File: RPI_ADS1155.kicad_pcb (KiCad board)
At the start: 2 copper layers, 84.6 x 56 mm, 28 parts, among them J1 Raspberry_PI_4, J2 DIGITAL_BITS, SW1 SW_DIP_x04, SW2 SW_Push, SW3 SW_Push, U1 ADS1115IDGS

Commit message: Add files via upload
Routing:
- net /+3.3V: track 126.3 -> 244.3 mm, vias 0 -> 2
- net /AINO: track 26.8 -> 27.7 mm
- net /AIN1: track 29.1 -> 30.1 mm

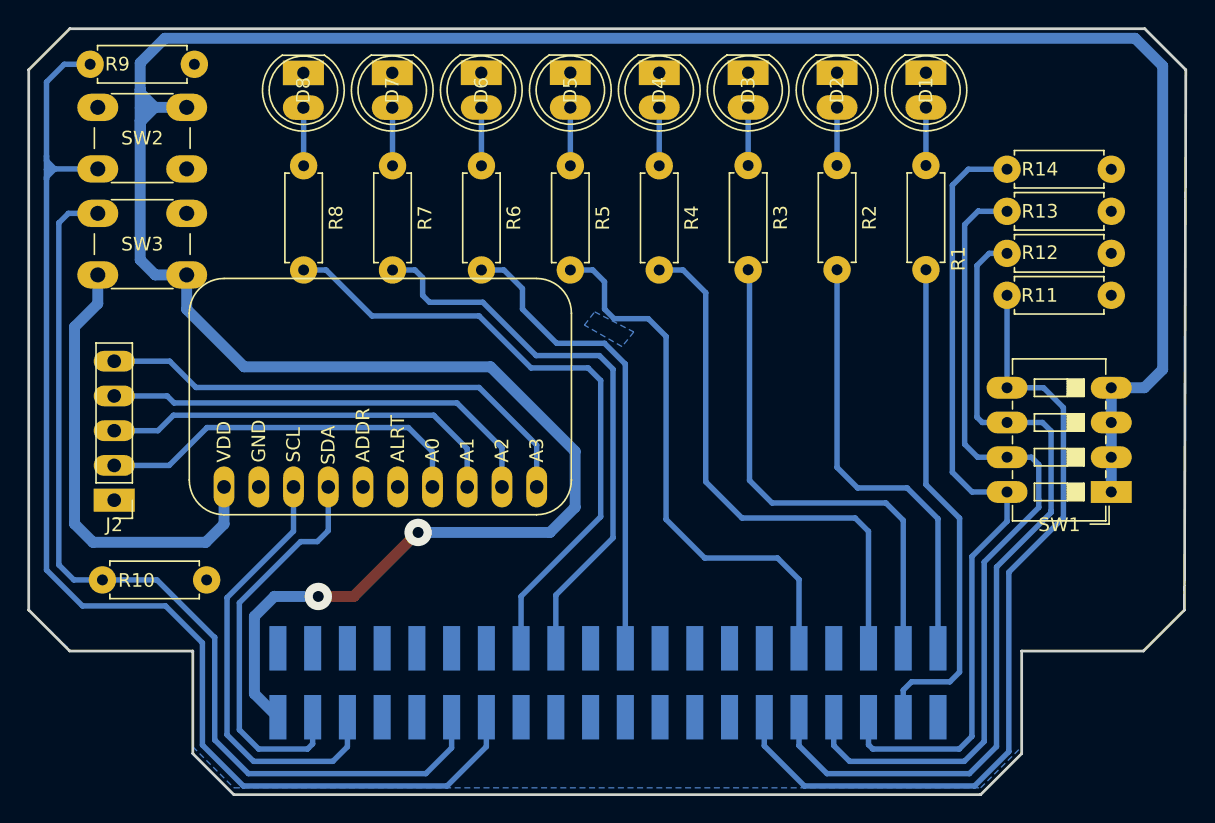
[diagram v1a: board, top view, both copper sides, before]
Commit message: Add UART connector and pins
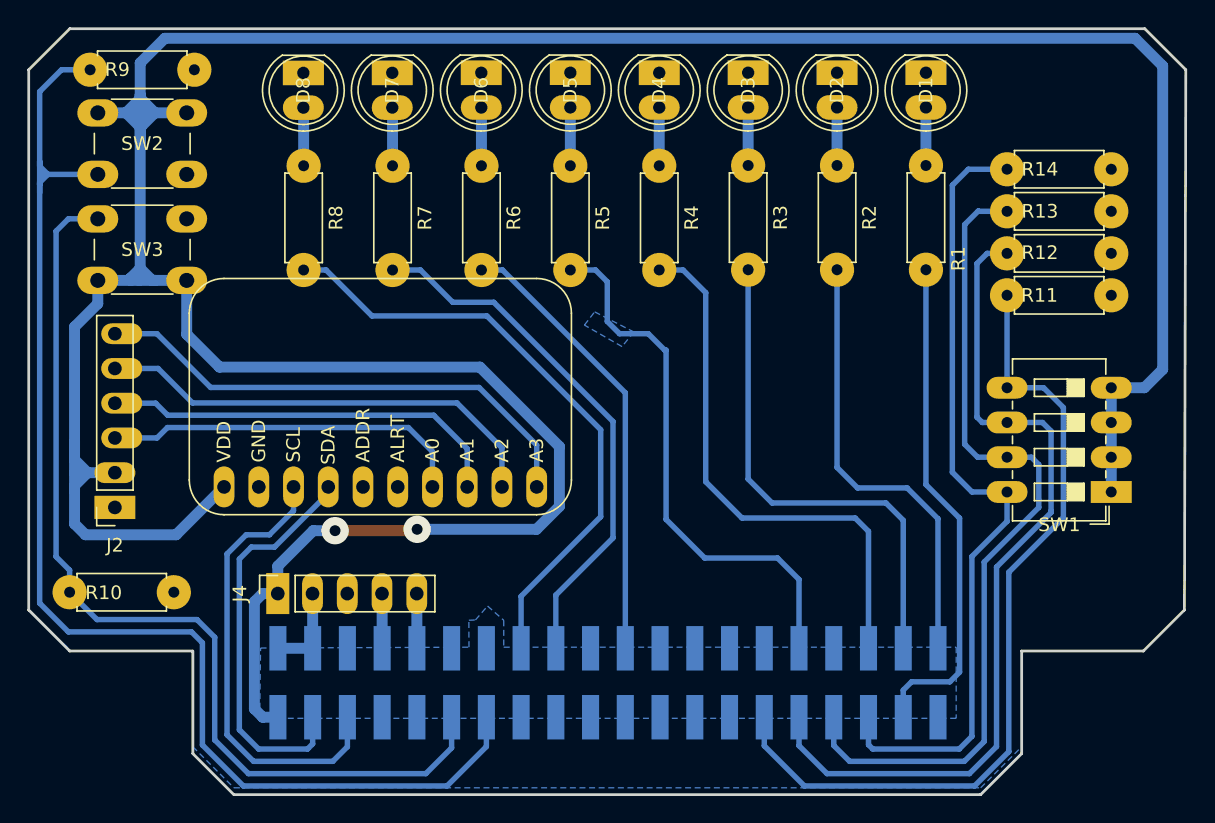
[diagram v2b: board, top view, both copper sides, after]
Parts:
- added J4: UART_PINS, Connector_PinSocket_2.54mm:PinSocket_1x05_P2.54mm_Vertical, F.Cu at (129.6, 123.8)
- J2: value DIGITAL_BITS -> ANALOG_PINS; footprint Connector_PinHeader_2.54mm:PinHeader_1x05_P2.54mm_Vertical -> Connector_PinSocket_2.54mm:PinSocket_1x06_P2.54mm_Vertical
- moved R10 2.56 mm to (114.4, 123.7)
- moved J2 0.53 mm to (117.7, 117.5)
- moved R9 0.40 mm to (115.9, 85.5)
- moved SW2 0.40 mm to (116.5, 88.7)
- moved SW3 0.40 mm to (123.0, 100.9)
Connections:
- J1 pad 10: unconnected-(J1-Pin_10-Pad10) -> /Rx
- J1 pad 15: /+3.3V -> unconnected-(J1-Pin_15-Pad15)
- J1 pad 2: unconnected-(J1-Pin_2-Pad2) -> /+5V
- J1 pad 4: unconnected-(J1-Pin_4-Pad4) -> /+5V
- J1 pad 8: unconnected-(J1-Pin_8-Pad8) -> /Tx
- J2 pad 2: /AINO -> /+3.3V
- J2 pad 3: /AIN1 -> /AINO
- J2 pad 4: /AIN2 -> /AIN1
- J2 pad 5: /AIN3 -> /AIN2
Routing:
- net /+3.3V: track 244.3 -> 263.5 mm
- net /+5V: track 0.00 -> 6.54 mm
- net /Tx: track 0.00 -> 4.00 mm
- net /Rx: track 0.00 -> 4.00 mm
- net /GPIO27: track 91.8 -> 95.5 mm
- net /GPIO24: track 42.0 -> 39.0 mm
- net /GPIO23: track 47.1 -> 44.9 mm
- net /GPIO25: track 35.0 -> 32.9 mm
- net /SCL: track 32.3 -> 33.3 mm
- net /AINO: track 27.7 -> 26.8 mm
- net /AIN3: track 36.5 -> 37.3 mm
- net /AIN2: track 32.8 -> 33.6 mm
